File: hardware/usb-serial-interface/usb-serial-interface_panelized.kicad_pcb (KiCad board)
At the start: 2 copper layers, 100.1 x 99.2 mm, 114 parts, among them J1 USB_B, J2 RJ12, U1 CP2102N-A01-GQFN24

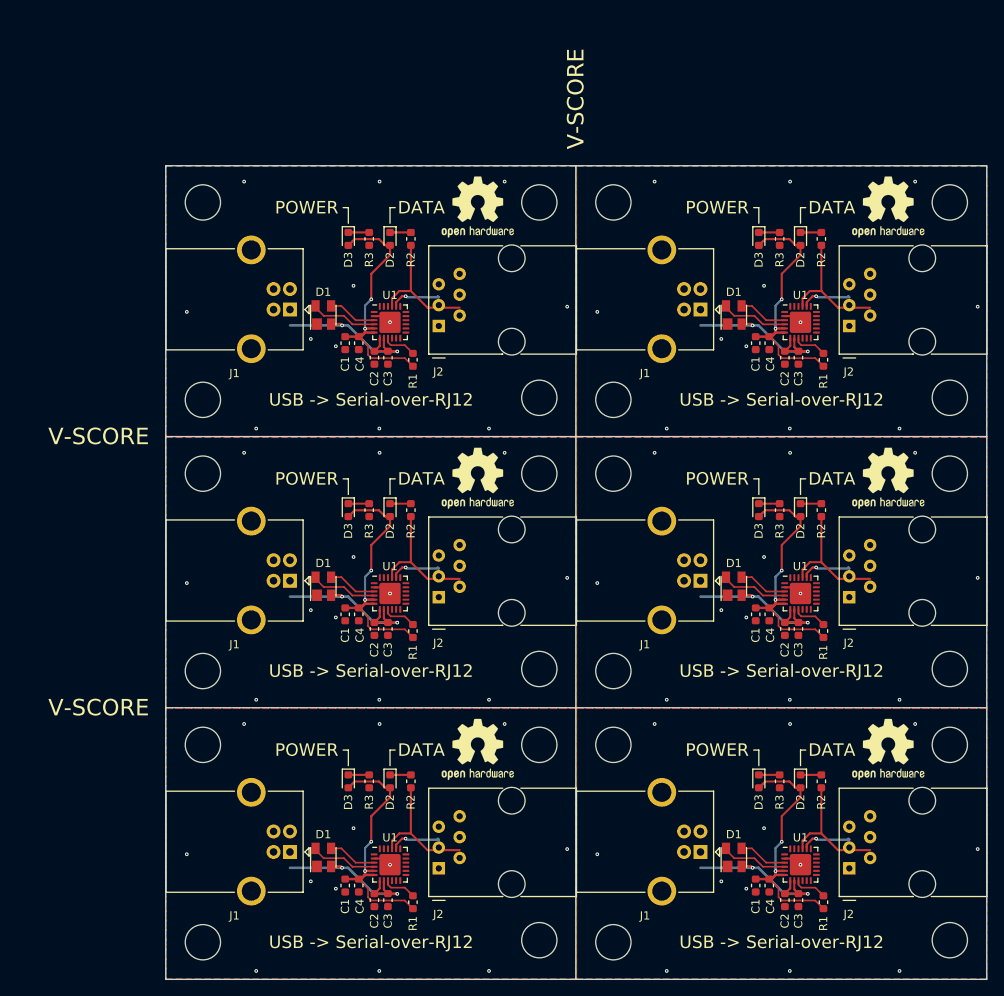
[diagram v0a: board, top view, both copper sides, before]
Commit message: New USB to serial board image
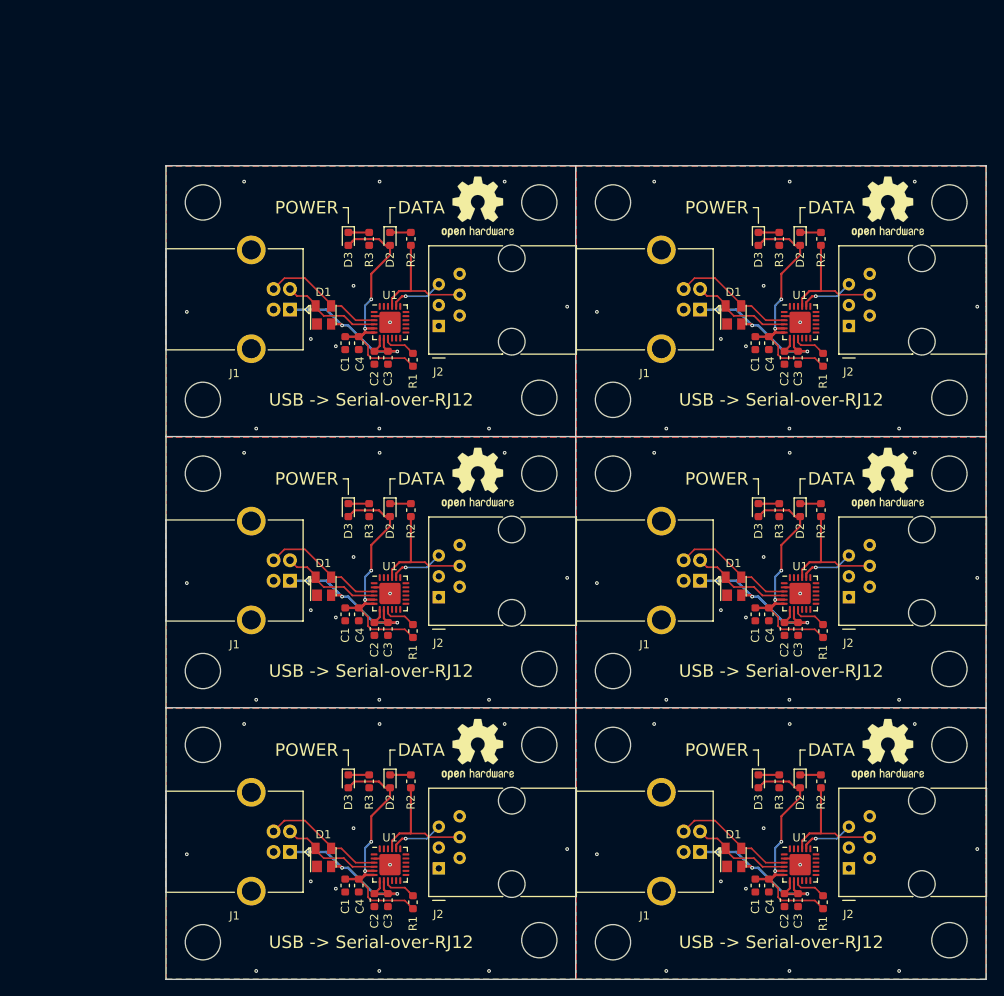
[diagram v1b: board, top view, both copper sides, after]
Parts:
- removed the C1 at (151.2, 151.8)
- removed the C1 at (151.2, 118.8)
- removed the C1 at (151.2, 85.7)
- removed the C2 at (154.8, 153.6)
- removed the C2 at (154.8, 120.6)
- removed the C2 at (154.8, 87.5)
- removed the C3 at (156.5, 153.6)
- removed the C3 at (156.5, 120.6)
- removed the C3 at (156.5, 87.5)
- removed the C4 at (152.9, 151.8)
- removed the C4 at (152.9, 118.8)
- removed the C4 at (152.9, 85.7)
- removed the D1 at (148.6, 148.4)
- removed the D1 at (148.6, 115.3)
- removed the D1 at (148.6, 82.3)
- removed the D2 at (156.7, 139.1)
- removed the D2 at (156.7, 106.1)
- removed the D2 at (156.7, 73.0)
- removed the D3 at (151.6, 139.1)
- removed the D3 at (151.6, 106.1)
- removed the D3 at (151.6, 73.0)
- removed the J1 at (144.5, 147.7)
- removed the J1 at (144.5, 114.7)
- removed the J1 at (144.5, 81.6)
- removed the J2 at (162.7, 149.7)
- removed the J2 at (162.7, 116.7)
- removed the J2 at (162.7, 83.6)
- removed the R1 at (159.5, 153.9)
- removed the R1 at (159.5, 120.8)
- removed the R1 at (159.5, 87.8)
- removed the R2 at (159.2, 139.1)
- removed the R2 at (159.2, 106.1)
- removed the R2 at (159.2, 73.0)
- removed the R3 at (154.2, 139.1)
- removed the R3 at (154.2, 106.1)
- removed the R3 at (154.2, 73.0)
- removed the REF** at (133.9, 134.7)
- removed the REF** at (174.9, 134.7)
- removed the REF** at (174.9, 101.6)
- removed the REF** at (174.9, 68.6)
- removed the REF** at (174.9, 158.5)
- removed the REF** at (174.9, 125.4)
- removed the REF** at (174.9, 92.4)
- removed the REF** at (133.9, 101.6)
- removed the REF** at (135.1, 148.0)
- removed the REF** at (135.1, 115.0)
- removed the REF** at (135.1, 81.9)
- removed the REF** at (167.4, 135.2)
- removed the REF** at (167.4, 102.2)
- removed the REF** at (167.4, 69.1)
- removed the REF** at (133.9, 68.6)
- removed the REF** at (133.9, 158.7)
- removed the REF** at (133.9, 125.7)
- removed the REF** at (133.9, 92.6)
- removed the U1 at (156.7, 149.3)
- removed the U1 at (156.7, 116.2)
- removed the U1 at (156.7, 83.2)
- added C1: 4.7u, Capacitor_SMD:C_0603_1608Metric, F.Cu at (151.2, 151.8)
- added C1: 4.7u, Capacitor_SMD:C_0603_1608Metric, F.Cu at (151.2, 118.8)
- added C1: 4.7u, Capacitor_SMD:C_0603_1608Metric, F.Cu at (151.2, 85.7)
- added C2: 4.7u, Capacitor_SMD:C_0603_1608Metric, F.Cu at (154.8, 153.6)
- added C2: 4.7u, Capacitor_SMD:C_0603_1608Metric, F.Cu at (154.8, 120.6)
- added C2: 4.7u, Capacitor_SMD:C_0603_1608Metric, F.Cu at (154.8, 87.5)
- added C3: 0.1u, Capacitor_SMD:C_0603_1608Metric, F.Cu at (156.4, 153.6)
- added C3: 0.1u, Capacitor_SMD:C_0603_1608Metric, F.Cu at (156.4, 120.6)
- added C3: 0.1u, Capacitor_SMD:C_0603_1608Metric, F.Cu at (156.4, 87.5)
- added C4: 0.1u, Capacitor_SMD:C_0603_1608Metric, F.Cu at (152.8, 151.8)
- added C4: 0.1u, Capacitor_SMD:C_0603_1608Metric, F.Cu at (152.8, 118.8)
- added C4: 0.1u, Capacitor_SMD:C_0603_1608Metric, F.Cu at (152.8, 85.7)
- added D1: SP0503BAHT, Package_TO_SOT_SMD:SOT-143, F.Cu at (148.5, 148.4)
- added D1: SP0503BAHT, Package_TO_SOT_SMD:SOT-143, F.Cu at (148.5, 115.3)
- added D1: SP0503BAHT, Package_TO_SOT_SMD:SOT-143, F.Cu at (148.5, 82.3)
- added D2: LED, LED_SMD:LED_0603_1608Metric, F.Cu at (156.7, 139.1)
- added D2: LED, LED_SMD:LED_0603_1608Metric, F.Cu at (156.7, 106.1)
- added D2: LED, LED_SMD:LED_0603_1608Metric, F.Cu at (156.7, 73.0)
- added D3: LED, LED_SMD:LED_0603_1608Metric, F.Cu at (151.6, 139.1)
- added D3: LED, LED_SMD:LED_0603_1608Metric, F.Cu at (151.6, 106.1)
- added D3: LED, LED_SMD:LED_0603_1608Metric, F.Cu at (151.6, 73.0)
- added J1: USB_B, Connector_USB:USB_B_OST_USB-B1HSxx_Horizontal, F.Cu at (144.5, 147.7)
- added J1: USB_B, Connector_USB:USB_B_OST_USB-B1HSxx_Horizontal, F.Cu at (144.5, 114.7)
- added J1: USB_B, Connector_USB:USB_B_OST_USB-B1HSxx_Horizontal, F.Cu at (144.5, 81.6)
- added J2: RJ12, footprints:RJ12_Amphenol_54601, F.Cu at (162.6, 149.7)
- added J2: RJ12, footprints:RJ12_Amphenol_54601, F.Cu at (162.6, 116.7)
- added J2: RJ12, footprints:RJ12_Amphenol_54601, F.Cu at (162.6, 83.6)
- added R1: 4.7k, Resistor_SMD:R_0603_1608Metric, F.Cu at (159.4, 153.9)
- added R1: 4.7k, Resistor_SMD:R_0603_1608Metric, F.Cu at (159.4, 120.8)
- added R1: 4.7k, Resistor_SMD:R_0603_1608Metric, F.Cu at (159.4, 87.8)
- added R2: 1k, Resistor_SMD:R_0603_1608Metric, F.Cu at (159.2, 139.1)
- added R2: 1k, Resistor_SMD:R_0603_1608Metric, F.Cu at (159.2, 106.1)
- added R2: 1k, Resistor_SMD:R_0603_1608Metric, F.Cu at (159.2, 73.0)
- added R3: 1k, Resistor_SMD:R_0603_1608Metric, F.Cu at (154.1, 139.1)
- added R3: 1k, Resistor_SMD:R_0603_1608Metric, F.Cu at (154.1, 106.1)
- added R3: 1k, Resistor_SMD:R_0603_1608Metric, F.Cu at (154.1, 73.0)
- added REF**: MountingHole_4.3mm_M4, MountingHole:MountingHole_4.3mm_M4, F.Cu at (133.9, 134.7)
- added REF**: MountingHole_4.3mm_M4, MountingHole:MountingHole_4.3mm_M4, F.Cu at (174.9, 134.7)
- added REF**: MountingHole_4.3mm_M4, MountingHole:MountingHole_4.3mm_M4, F.Cu at (174.9, 101.6)
- added REF**: MountingHole_4.3mm_M4, MountingHole:MountingHole_4.3mm_M4, F.Cu at (174.9, 68.6)
- added REF**: MountingHole_4.3mm_M4, MountingHole:MountingHole_4.3mm_M4, F.Cu at (174.9, 158.5)
- added REF**: MountingHole_4.3mm_M4, MountingHole:MountingHole_4.3mm_M4, F.Cu at (174.9, 125.4)
- added REF**: MountingHole_4.3mm_M4, MountingHole:MountingHole_4.3mm_M4, F.Cu at (174.9, 92.4)
- added REF**: MountingHole_4.3mm_M4, MountingHole:MountingHole_4.3mm_M4, F.Cu at (133.9, 101.6)
- added REF**: OSHW-Logo2_9.8x8mm_SilkScreen, Symbol:OSHW-Logo2_9.8x8mm_SilkScreen, B.Cu at (135.1, 148.0)
- added REF**: OSHW-Logo2_9.8x8mm_SilkScreen, Symbol:OSHW-Logo2_9.8x8mm_SilkScreen, B.Cu at (135.1, 115.0)
- added REF**: OSHW-Logo2_9.8x8mm_SilkScreen, Symbol:OSHW-Logo2_9.8x8mm_SilkScreen, B.Cu at (135.1, 81.9)
- added REF**: OSHW-Logo2_9.8x8mm_SilkScreen, Symbol:OSHW-Logo2_9.8x8mm_SilkScreen, F.Cu at (167.4, 135.2)
- added REF**: OSHW-Logo2_9.8x8mm_SilkScreen, Symbol:OSHW-Logo2_9.8x8mm_SilkScreen, F.Cu at (167.4, 102.2)
- added REF**: OSHW-Logo2_9.8x8mm_SilkScreen, Symbol:OSHW-Logo2_9.8x8mm_SilkScreen, F.Cu at (167.4, 69.1)
- added REF**: MountingHole_4.3mm_M4, MountingHole:MountingHole_4.3mm_M4, F.Cu at (133.9, 68.6)
- added REF**: MountingHole_4.3mm_M4, MountingHole:MountingHole_4.3mm_M4, F.Cu at (133.9, 158.7)
- added REF**: MountingHole_4.3mm_M4, MountingHole:MountingHole_4.3mm_M4, F.Cu at (133.9, 125.7)
- added REF**: MountingHole_4.3mm_M4, MountingHole:MountingHole_4.3mm_M4, F.Cu at (133.9, 92.6)
- added U1: CP2102N-A01-GQFN24, Package_DFN_QFN:QFN-24-1EP_4x4mm_P0.5mm_EP2.6x2.6mm, F.Cu at (156.7, 149.3)
- added U1: CP2102N-A01-GQFN24, Package_DFN_QFN:QFN-24-1EP_4x4mm_P0.5mm_EP2.6x2.6mm, F.Cu at (156.7, 116.2)
- added U1: CP2102N-A01-GQFN24, Package_DFN_QFN:QFN-24-1EP_4x4mm_P0.5mm_EP2.6x2.6mm, F.Cu at (156.7, 83.2)
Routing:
- net /D+: track 35.8 -> 90.3 mm
- net /D-: track 49.1 -> 73.6 mm
- net VBUS: track 133.6 -> 138.4 mm
- net /TXD: track 96.0 -> 92.0 mm
- net /RXD: track 37.4 -> 39.7 mm
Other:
- board size 100.1 x 99.2 mm -> 100 x 99.2 mm
- board text added: "/home/willem/Documents/GitHub/midi-solenoid-driver/hardware/usb-serial-interface/usb-serial-interface_panelized.kicad_pcb (2x3 panel) generated with: ./panelizer.py --panely 100 --panelx 100 /home/willem/Documents/GitHub/midi-solenoid-driver/hardware/usb-serial-interface/usb-serial-interface.kicad_pcb"
- board text added: "Willem Hillier rev2.1 19.224"
- board text removed: "/home/willem/Documents/GitHub/midi-solenoid-driver/hardware/usb-serial-interface/usb-serial-interface_panelized.kicad_pcb (2x3 panel) generated with: ./panelizer.py --panely 100 --panelx 101 --vscorelayer Edge.Cuts --vscoretextlayer F.SilkS /home/willem/Documents/GitHub/midi-solenoid-driver/hardware/usb-serial-interface/usb-serial-interface.kicad_pcb"
- board text removed: "Willem Hillier rev2 19.222"
